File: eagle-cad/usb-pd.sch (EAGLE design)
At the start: 24 parts, among them Q1 CERAMIC_RESONATOR_SMD6M00G53Z, U1 ATMEGA328-AU

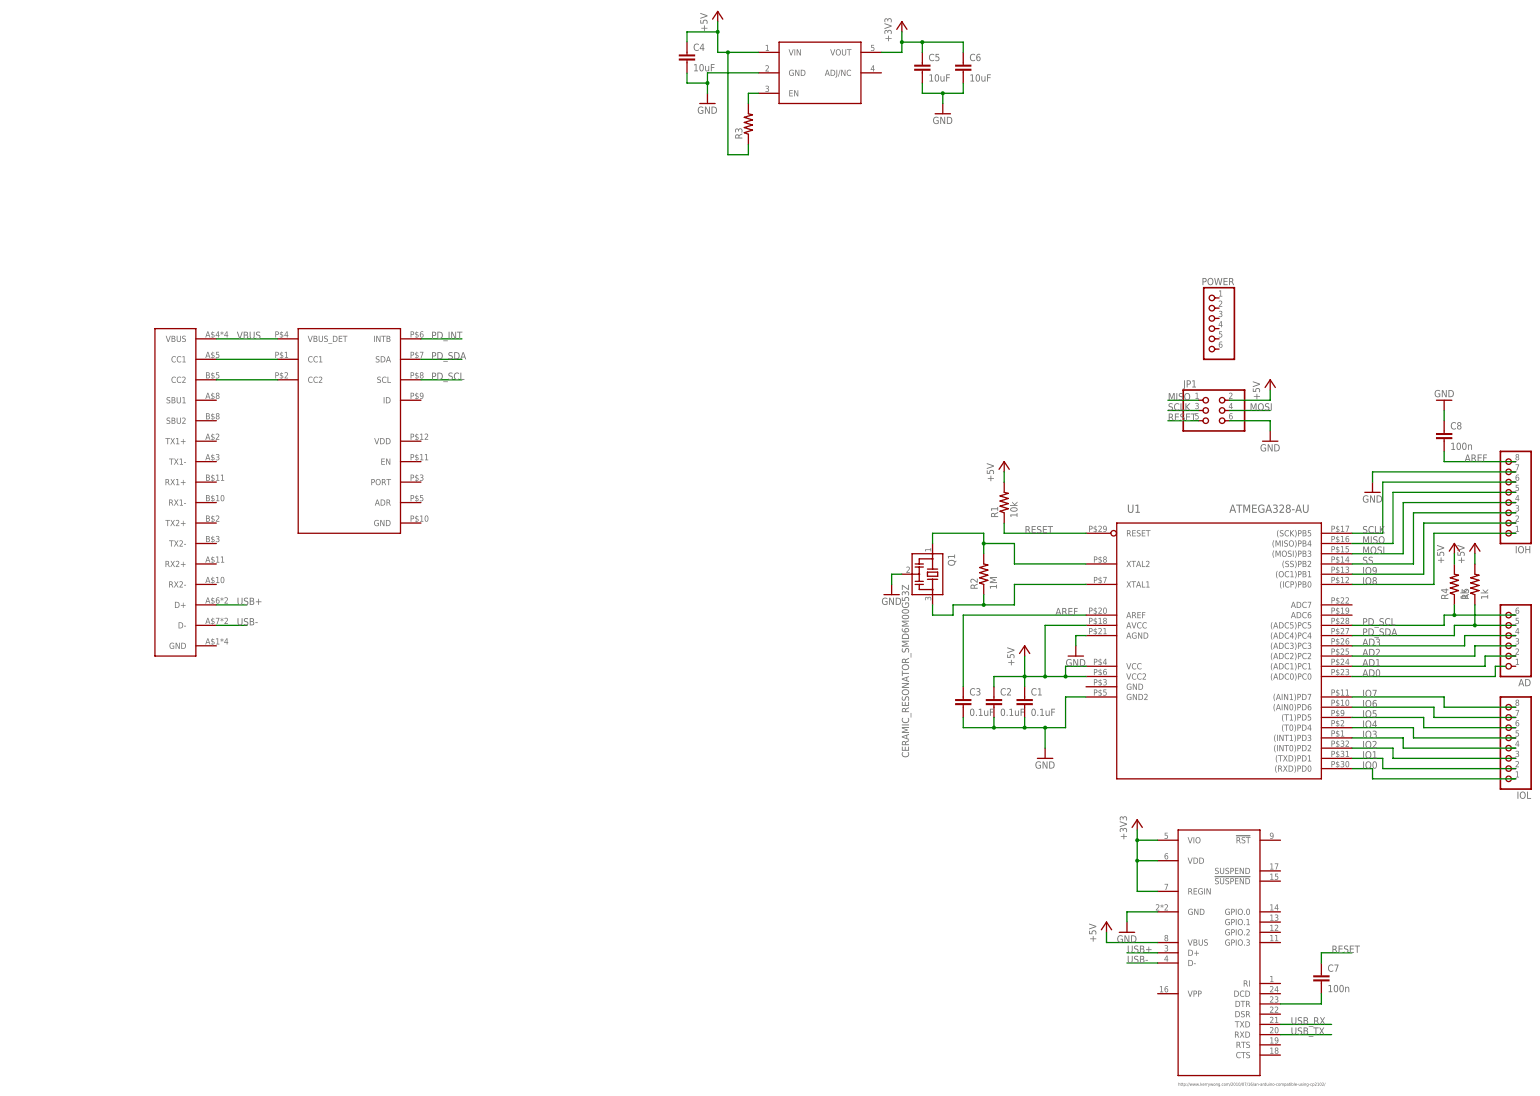
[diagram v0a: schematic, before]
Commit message: Filled out PTN5150, arranged board like an Uno rev3
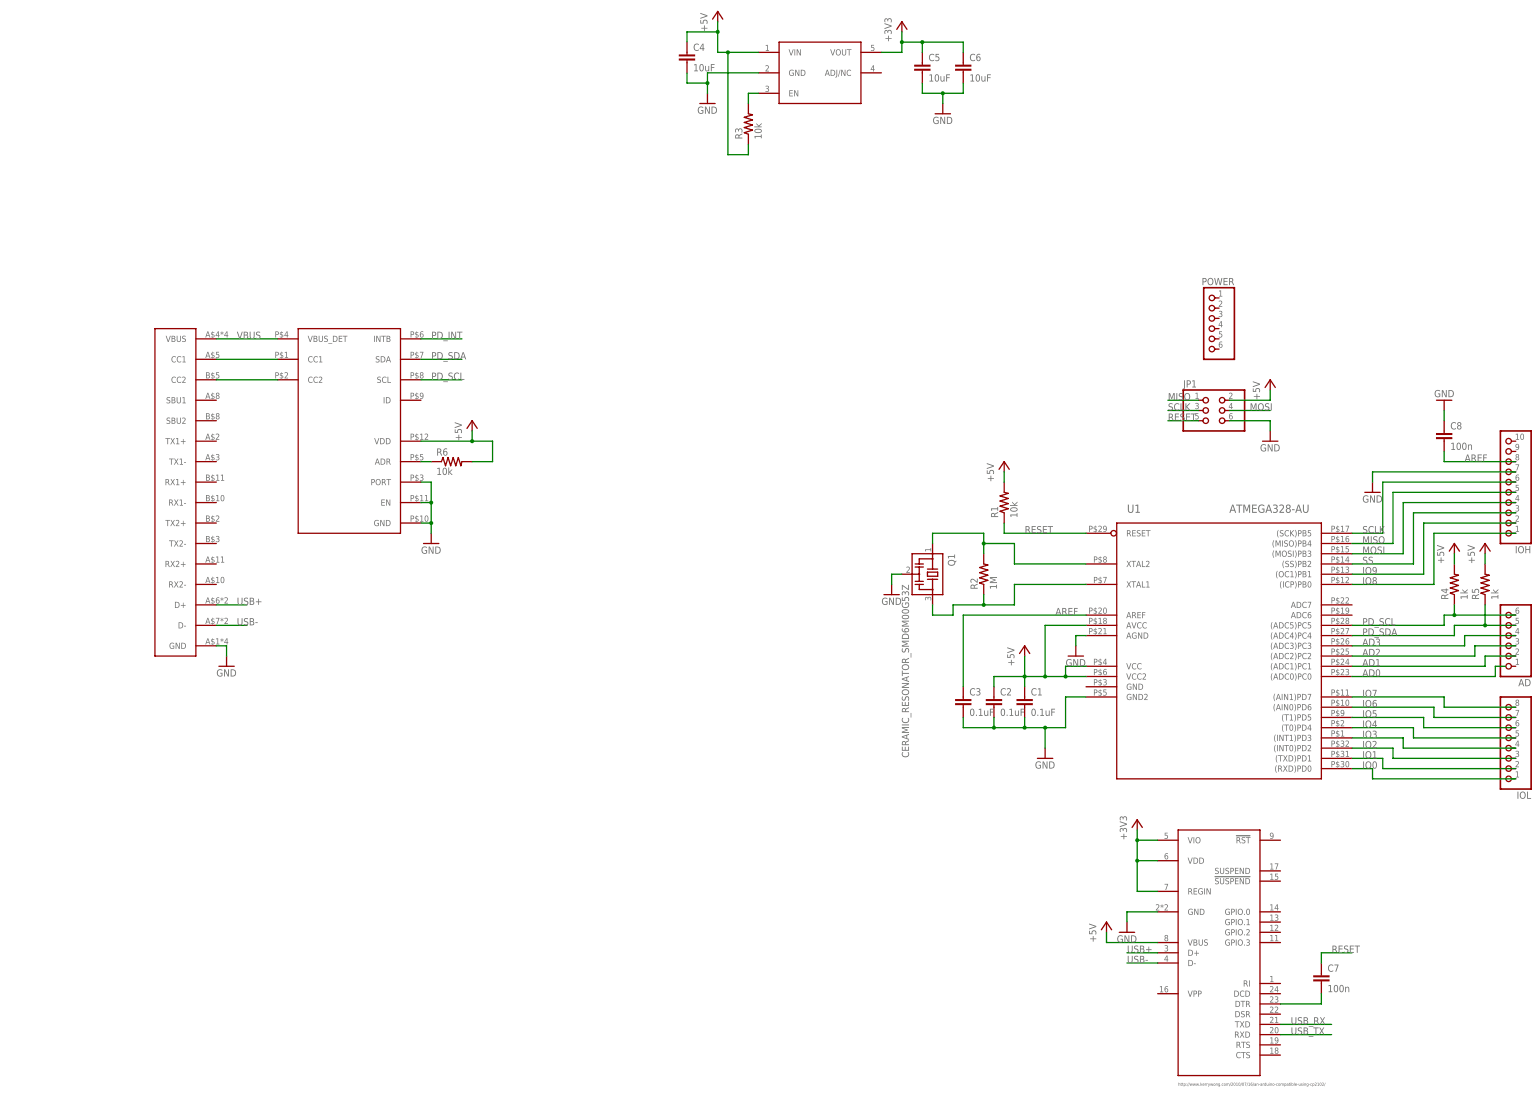
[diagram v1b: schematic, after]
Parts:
- added R6: 10k, rcl:R-US_R0805
- IOH: device pinhead:PINHD-1X8 -> pinhead:PINHD-1X10
- R3: value (none) -> 10k
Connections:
- new net N$8: R6.1, U$3.ADR
- net +5V: now also R6.2, U$3.VDD
- net GND: now also U$1.GND, U$3.EN, U$3.GND, U$3.PORT
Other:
- moved on the sheet: R5
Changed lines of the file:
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@@
 <part name="U1" library="usb-pd" deviceset="ATMEGA328-AU" device=""/>
 <part name="JP1" library="pinhead" deviceset="PINHD-2X3" device=""/>
-<part name="IOH" library="pinhead" deviceset="PINHD-1X8" device=""/>
+<part name="IOH" library="pinhead" deviceset="PINHD-1X10" device=""/>
 <part name="IOL" library="pinhead" deviceset="PINHD-1X8" device=""/>
 <part name="POWER" library="pinhead" deviceset="PINHD-1X6" device=""/>
@@
 <part name="C5" library="rcl" deviceset="C-EU" device="C0805" value="10uF"/>
 <part name="C6" library="rcl" deviceset="C-EU" device="C0805" value="10uF"/>
-<part name="R3" library="rcl" deviceset="R-US_" device="R0805"/>
+<part name="R3" library="rcl" deviceset="R-US_" device="R0805" value="10k"/>
 <part name="+3V2" library="supply1" deviceset="+3V3" device=""/>
 <part name="GND7" library="supply1" deviceset="GND" device=""/>
@@
 <part name="C8" library="rcl" deviceset="C-EU" device="C0805" value="100n"/>
 <part name="GND9" library="supply1" deviceset="GND" device=""/>
+<part name="GND10" library="supply1" deviceset="GND" device=""/>
+<part name="GND11" library="supply1" deviceset="GND" device=""/>
+<part name="P+8" library="supply1" deviceset="+5V" device=""/>
+<part name="R6" library="rcl" deviceset="R-US_" device="R0805" value="10k"/>
 </parts>
 <sheets>
@@
 <instance part="C7" gate="G$1" x="187.96" y="-40.64"/>
 <instance part="R4" gate="G$1" x="220.98" y="55.88" rot="R90"/>
-<instance part="R5" gate="G$1" x="226.06" y="55.88" rot="R90"/>
+<instance part="R5" gate="G$1" x="228.6" y="55.88" rot="R90"/>
 <instance part="P+6" gate="1" x="220.98" y="66.04"/>
-<instance part="P+7" gate="1" x="226.06" y="66.04"/>
+<instance part="P+7" gate="1" x="228.6" y="66.04"/>
 <instance part="AD" gate="A" x="233.68" y="43.18" rot="R180"/>
 <instance part="GND8" gate="1" x="200.66" y="78.74"/>
 <instance part="C8" gate="G$1" x="218.44" y="93.98"/>
 <instance part="GND9" gate="1" x="218.44" y="101.6" rot="R180"/>
+<instance part="GND10" gate="1" x="-83.82" y="35.56"/>
+<instance part="GND11" gate="1" x="-33.02" y="66.04"/>
+<instance part="P+8" gate="1" x="-22.86" y="96.52"/>
+<instance part="R6" gate="G$1" x="-27.94" y="86.36"/>
 </instances>
 <busses>
@@
 <pinref part="R5" gate="G$1" pin="2"/>
 <pinref part="P+7" gate="1" pin="+5V"/>
-<wire x1="226.06" y1="63.5" x2="226.06" y2="60.96" width="0.1524" layer="91"/>
+<wire x1="228.6" y1="63.5" x2="228.6" y2="60.96" width="0.1524" layer="91"/>
+</segment>
+<segment>
+<pinref part="U$3" gate="G$1" pin="VDD"/>
+<pinref part="P+8" gate="1" pin="+5V"/>
+<wire x1="-35.56" y1="91.44" x2="-22.86" y2="91.44" width="0.1524" layer="91"/>
+<wire x1="-22.86" y1="91.44" x2="-22.86" y2="93.98" width="0.1524" layer="91"/>
+<pinref part="R6" gate="G$1" pin="2"/>
+<wire x1="-22.86" y1="86.36" x2="-17.78" y2="86.36" width="0.1524" layer="91"/>
+<wire x1="-17.78" y1="86.36" x2="-17.78" y2="91.44" width="0.1524" layer="91"/>
+<wire x1="-17.78" y1="91.44" x2="-22.86" y2="91.44" width="0.1524" layer="91"/>
+<junction x="-22.86" y="91.44"/>
 </segment>
 </net>
@@
 <pinref part="GND9" gate="1" pin="GND"/>
 </segment>
+<segment>
+<pinref part="U$1" gate="G$1" pin="GND"/>
+<pinref part="GND10" gate="1" pin="GND"/>
+<wire x1="-86.36" y1="40.64" x2="-83.82" y2="40.64" width="0.1524" layer="91"/>
+<wire x1="-83.82" y1="40.64" x2="-83.82" y2="38.1" width="0.1524" layer="91"/>
+</segment>
+<segment>
+<pinref part="U$3" gate="G$1" pin="GND"/>
+<pinref part="GND11" gate="1" pin="GND"/>
+<wire x1="-35.56" y1="71.12" x2="-33.02" y2="71.12" width="0.1524" layer="91"/>
+<wire x1="-33.02" y1="71.12" x2="-33.02" y2="68.58" width="0.1524" layer="91"/>
+<pinref part="U$3" gate="G$1" pin="EN"/>
+<wire x1="-35.56" y1="76.2" x2="-33.02" y2="76.2" width="0.1524" layer="91"/>
+<wire x1="-33.02" y1="76.2" x2="-33.02" y2="71.12" width="0.1524" layer="91"/>
+<junction x="-33.02" y="71.12"/>
+<pinref part="U$3" gate="G$1" pin="PORT"/>
+<wire x1="-35.56" y1="81.28" x2="-33.02" y2="81.28" width="0.1524" layer="91"/>
+<wire x1="-33.02" y1="81.28" x2="-33.02" y2="76.2" width="0.1524" layer="91"/>
+<junction x="-33.02" y="76.2"/>
+</segment>
 </net>
 <net name="AREF" class="0">
@@
 <label x="198.12" y="43.18" size="1.778" layer="95"/>
 <pinref part="AD" gate="A" pin="5"/>
-<wire x1="236.22" y1="45.72" x2="226.06" y2="45.72" width="0.1524" layer="91"/>
+<wire x1="236.22" y1="45.72" x2="228.6" y2="45.72" width="0.1524" layer="91"/>
 <pinref part="R5" gate="G$1" pin="1"/>
-<wire x1="226.06" y1="45.72" x2="220.98" y2="45.72" width="0.1524" layer="91"/>
-<wire x1="226.06" y1="45.72" x2="226.06" y2="50.8" width="0.1524" layer="91"/>
-<junction x="226.06" y="45.72"/>
+<wire x1="228.6" y1="45.72" x2="220.98" y2="45.72" width="0.1524" layer="91"/>
+<wire x1="228.6" y1="45.72" x2="228.6" y2="50.8" width="0.1524" layer="91"/>
+<junction x="228.6" y="45.72"/>
 <wire x1="220.98" y1="45.72" x2="220.98" y2="43.18" width="0.1524" layer="91"/>
 <pinref part="U1" gate="G$1" pin="(ADC4)PC4"/>
@@
 </segment>
 </net>
+<net name="N$8" class="0">
+<segment>
+<pinref part="R6" gate="G$1" pin="1"/>
+<pinref part="U$3" gate="G$1" pin="ADR"/>
+<wire x1="-35.56" y1="86.36" x2="-33.02" y2="86.36" width="0.1524" layer="91"/>
+</segment>
+</net>

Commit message: Added 5V buck implementation (need power FET to control it)
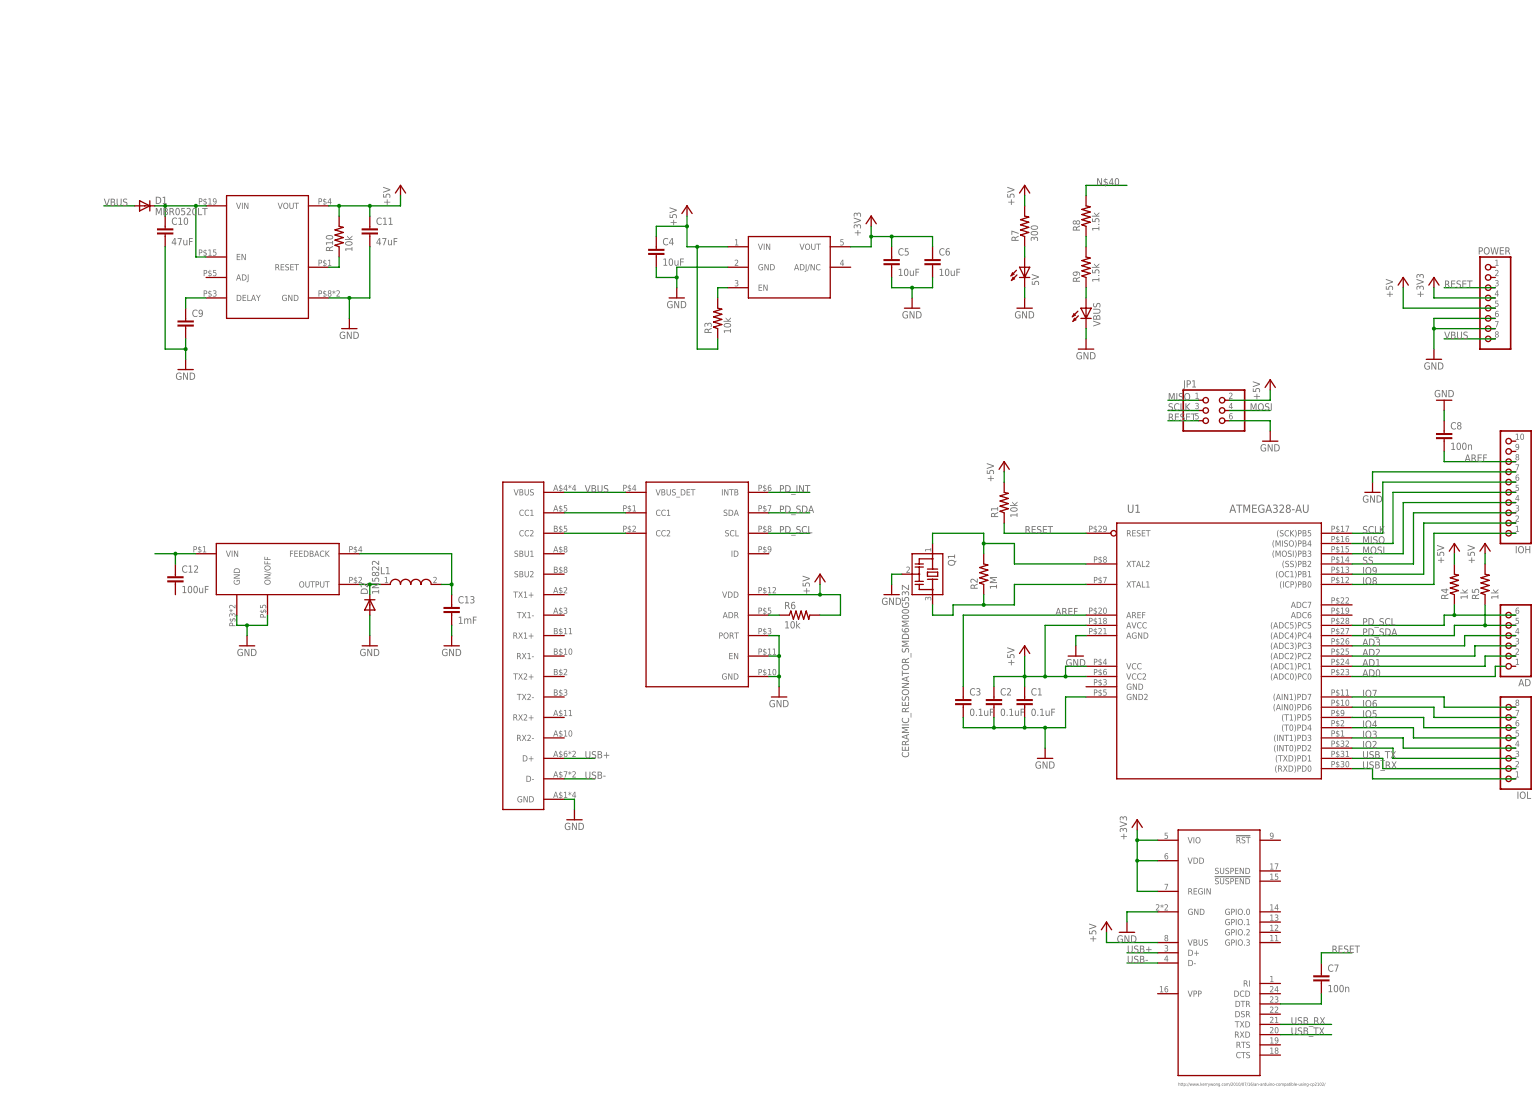
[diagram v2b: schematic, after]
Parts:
- added 5V, VBUS: (no value), led:LEDCHIPLED_0603
- added C10, C11: 47uF, rcl:C-EUC0805
- added C12: 100uF, rcl:C-EUC0805
- added C13: 1mF, rcl:C-EUC0805
- added C9: (no value), rcl:C-EUC0805
- added D1: MBR0520LT, diode:MBR0520LT
- added D2: 1N5822, diode:1N5400
- added L1: (no value), EagleLibrary_Wuerth_Elektronik_eiSos_rev16a:WE-RFI_0805
- added R10: 10k, rcl:R-US_R0805
- added R7: 300, rcl:R-US_R0805
- added R8, R9: 1.5k, rcl:R-US_R0805
- added U$2: TI-TPS7B6750-Q1, usb-pd:TI-TPS7B6750-Q1
- added U$6: TI-LM2576-5.0, usb-pd:TI-LM2576-5.0
- POWER: device pinhead:PINHD-1X6 -> pinhead:PINHD-1X8
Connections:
- removed net IO0: IOL.1, U1.(RXD)PD0
- removed net IO1: IOL.2, U1.(TXD)PD1
- new net N$1: C12.1, U$6.VIN
- new net N$10: 5V.A, R7.1
- new net N$11: R9.1, VBUS.A
- new net N$12: R8.1, R9.2
- new net N$13: R10.1, U$2.RESET
- new net N$14: C9.1, U$2.DELAY
- new net N$15: C13.1, L1.2, U$6.FEEDBACK
- new net N$40: C10.1, D1.C, R8.2, U$2.EN, U$2.VIN
- new net N$9: D2.C, L1.1, U$6.OUTPUT
- net +3V3: now also POWER.4
- net +5V: now also C11.1, POWER.5, R10.2, R7.2, U$2.VOUT
- net GND: now also 5V.C, C10.2, C11.2, C13.2, C9.2, D2.A, POWER.6, POWER.7, U$2.GND, U$6.GND, U$6.ON/OFF, VBUS.C
- net RESET: now also POWER.3
- net USB_RX: now also IOL.1, U1.(RXD)PD0
- net USB_TX: now also IOL.2, U1.(TXD)PD1
- net VBUS: now also D1.A, POWER.8
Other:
- moved on the sheet: C4, C5, C6, R3, R6
